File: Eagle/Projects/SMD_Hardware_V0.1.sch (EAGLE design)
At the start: 3 parts, among them IC1 LM386M-1

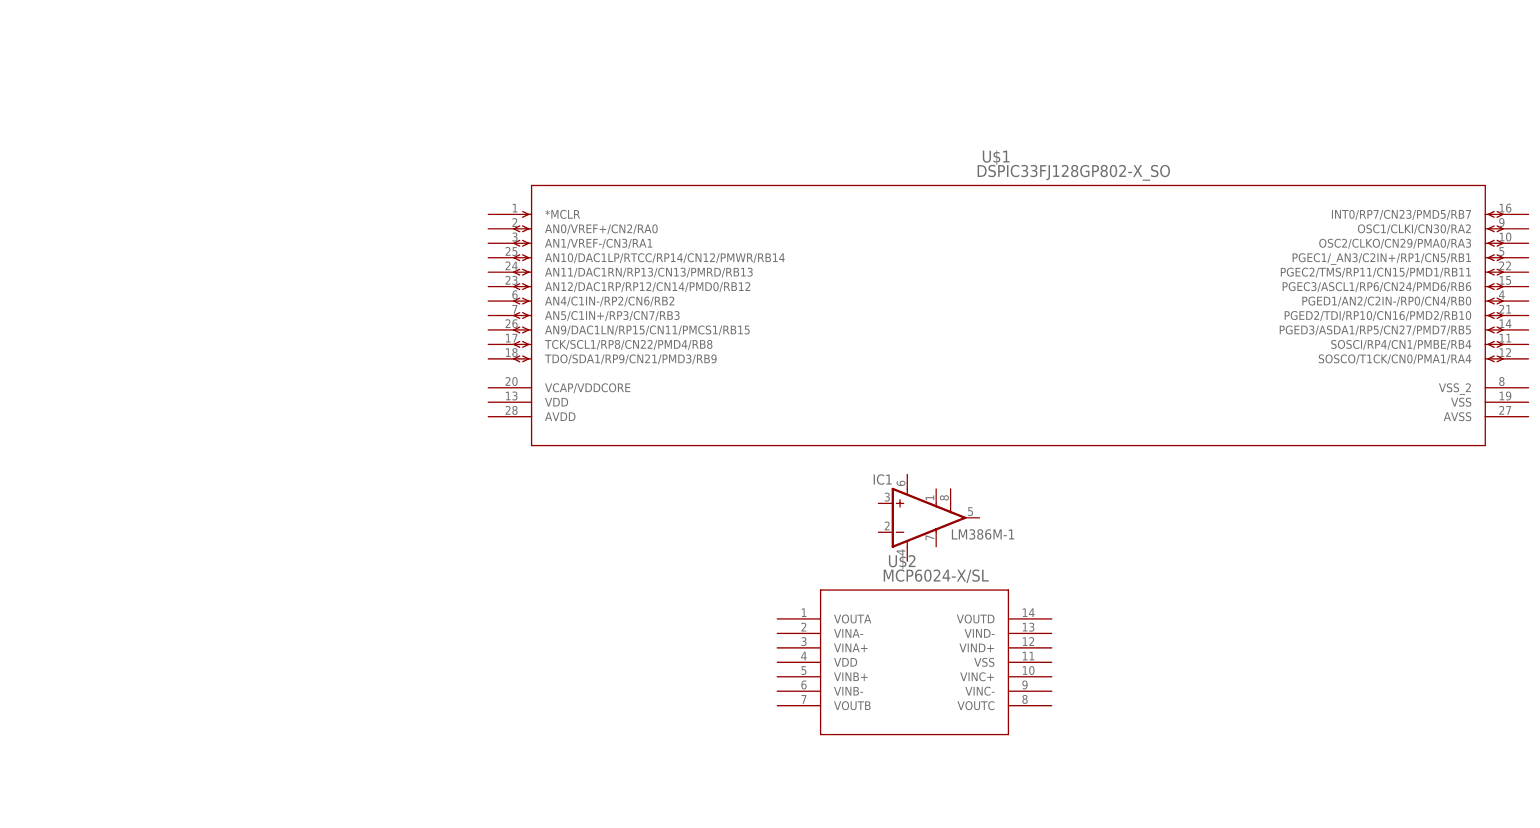
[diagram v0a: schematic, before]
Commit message: Layed out the board a bit more, finished off some connections for the basic micro layout.  Need to add a power supply yet
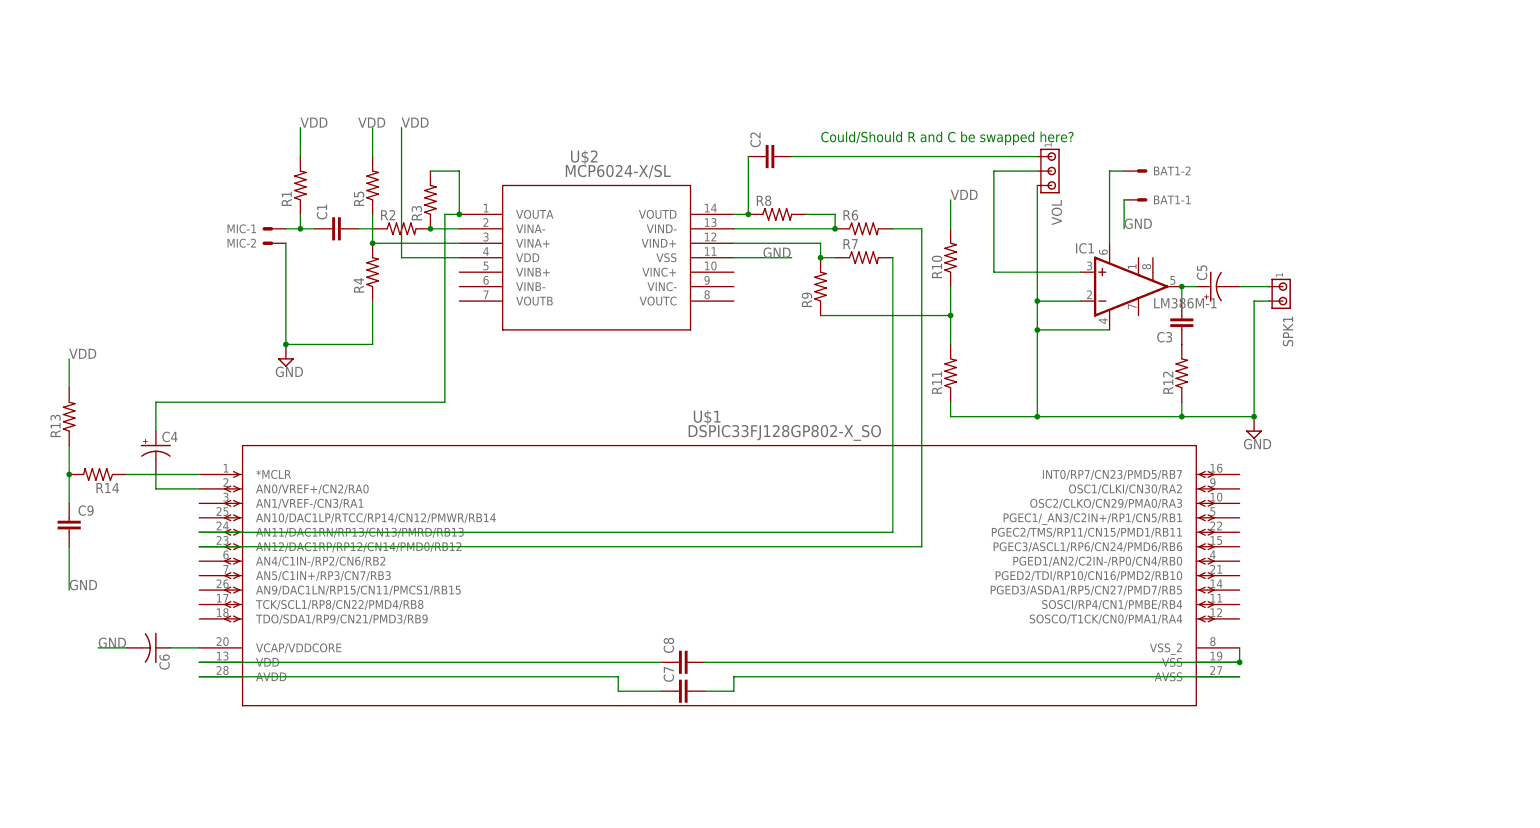
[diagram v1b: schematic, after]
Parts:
- added BAT1, MIC: 22-23-2021, con-molex:22-23-2021
- added C1, C2, C3: (no value), resistor:C-EUC0603
- added C4, C5: (no value), resistor:CPOL-US140CLH-0810
- added C6: (no value), resistor:C-USC0805
- added C7, C8, C9: (no value), resistor:C-EUC0805
- added R1, R10, R11, R12, R13, R14, R2, R3, R4, R5, R6, R7, R8, R9: (no value), resistor:R-US_R0603
- added SPK1: (no value), con-amp:MTA02-100
- added VOL: (no value), con-amp:MTA03-100
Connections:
- new net GND: BAT1-1.S, C6.2, C9.2, IC1.-IN, IC1.GND, MIC-2.S, R11.1, R12.1, R4.1, SPK1.2, U$2.VSS, VOL.3
- new net N$1: C1.1, MIC-1.S, R1.1
- new net N$10: R7.1, R9.2, U$2.VIND+
- new net N$11: R6.2, U$1.AN12/DAC1RP/RP12/CN14/PMD0/RB12
- new net N$12: C4.-, U$1.AN0/VREF+/CN2/RA0
- new net N$13: BAT1-2.S, IC1.VS
- new net N$14: C2.2, VOL.1
- new net N$15: C3.2, C5.+, IC1.OUT
- new net N$16: C3.1, R12.2
- new net N$17: C5.-, SPK1.1
- new net N$18: C6.1, U$1.VCAP/VDDCORE
- new net N$19: C8.1, U$1.VDD
- new net N$2: C1.2, R2.1
- new net N$20: C8.2, U$1.VSS, U$1.VSS_2
- new net N$21: C7.1, U$1.AVDD
- new net N$22: C7.2, U$1.AVSS
- new net N$23: C9.1, R13.1, R14.2
- new net N$24: R14.1, U$1.*MCLR
- new net N$25: IC1.+IN, VOL.2
- new net N$3: R2.2, R3.1, U$2.VINA-
- new net N$4: R4.2, R5.1, U$2.VINA+
- new net N$5: R10.1, R11.2, R9.1
- new net N$6: C4.+, R3.2, U$2.VOUTA
- new net N$7: C2.1, R8.1, U$2.VOUTD
- new net N$8: R6.1, R8.2, U$2.VIND-
- new net N$9: R7.2, U$1.AN11/DAC1RN/RP13/CN13/PMRD/RB13
- new net VDD: R1.2, R10.2, R13.2, R5.2, U$2.VDD
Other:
- note added: "Could/Should R and C be swapped here?"
- moved on the sheet: IC1, U$1, U$2

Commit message: Started editing the eagle files with values from the breadboard, and was working on the code a bit more
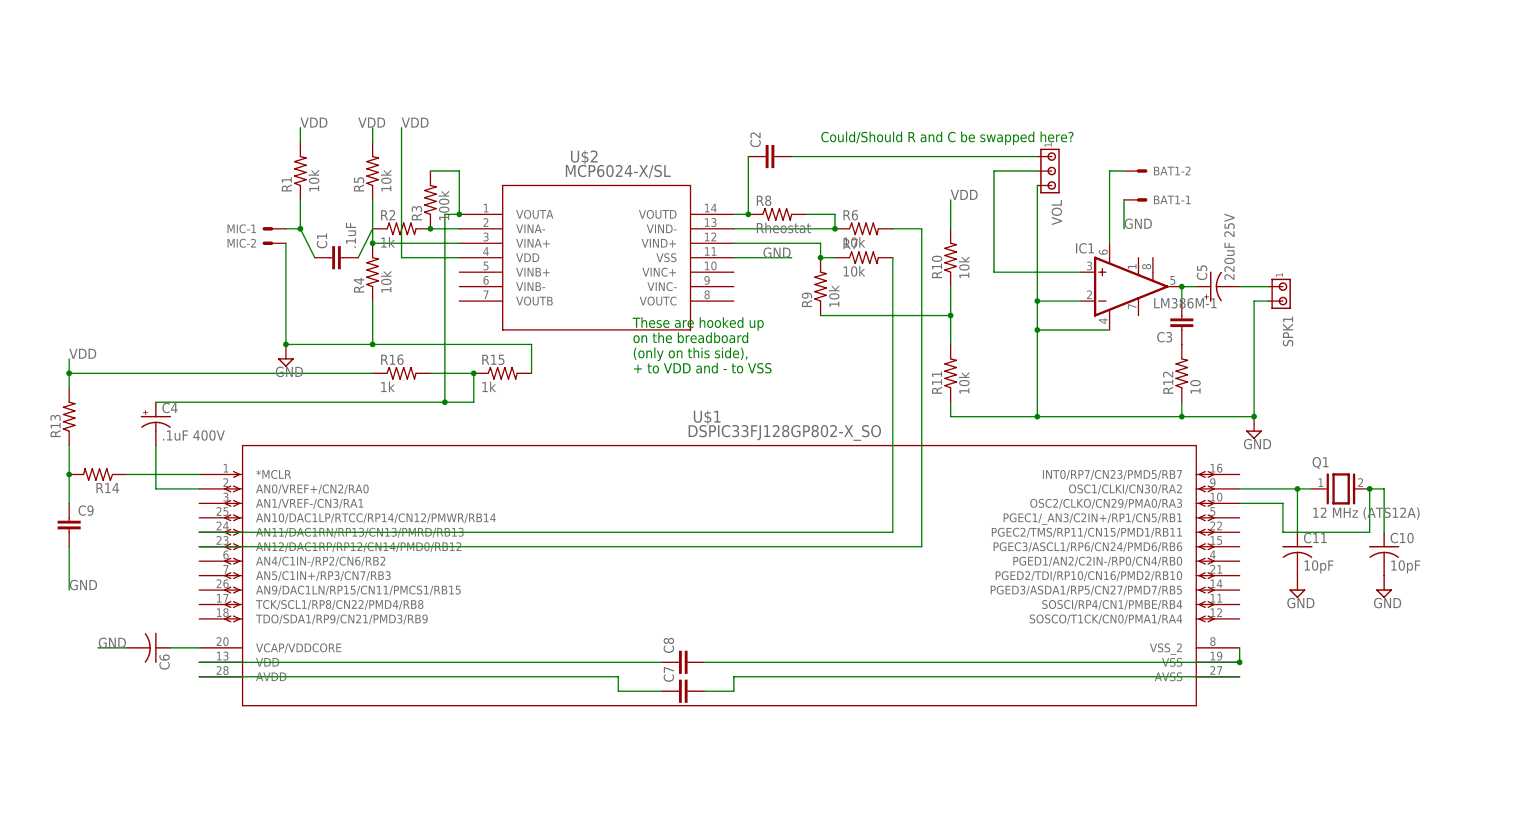
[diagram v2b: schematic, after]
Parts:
- added C10, C11: 10pF, resistor:C-US025-024X044
- added Q1: 12 MHz (ATS12A), special:XTAL
- added R15, R16: 1k, resistor:R-US_R0603
- C1: value (none) -> .1uF
- C4: value (none) -> .1uF 400V
- C5: value (none) -> 220uF 25V
- R1, R10, R11, R4, R5, R6, R7, R9: value (none) -> 10k
- R12: value (none) -> 10
- R2: value (none) -> 1k
- R3: value (none) -> 100k
- R8: value (none) -> Rheostat
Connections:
- removed net N$6: C4.+, R3.2, U$2.VOUTA
- new net N$26: C4.+, R15.1, R16.2, R3.2, U$2.VOUTA
- new net N$28: C11.1, Q1.1, U$1.OSC1/CLKI/CN30/RA2
- new net N$29: C10.1, Q1.2, U$1.OSC2/CLKO/CN29/PMA0/RA3
- net GND: now also C10.2, C11.2, R15.2
- net VDD: now also R16.1
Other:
- note added: "These are hooked up on the breadboard (only on this side), + to VDD and - to VSS"
- moved on the sheet: C1, C4, R1, R5

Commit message: Eagle changes
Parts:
- C9: value (none) -> DNI
- R13: value (none) -> 10k
- R14: value (none) -> 0 (short)
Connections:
- new net N$27: U$1.PGED1/AN2/C2IN-/RP0/CN4/RB0
- new net N$6: U$1.PGEC1/_AN3/C2IN+/RP1/CN5/RB1
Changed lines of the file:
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@@
 <part name="C7" library="resistor" deviceset="C-EU" device="C0805"/>
 <part name="C8" library="resistor" deviceset="C-EU" device="C0805"/>
-<part name="C9" library="resistor" deviceset="C-EU" device="C0805"/>
-<part name="R13" library="resistor" deviceset="R-US_" device="R0603"/>
-<part name="R14" library="resistor" deviceset="R-US_" device="R0603"/>
+<part name="C9" library="resistor" deviceset="C-EU" device="C0805" value="DNI"/>
+<part name="R13" library="resistor" deviceset="R-US_" device="R0603" value="10k"/>
+<part name="R14" library="resistor" deviceset="R-US_" device="R0603" value="0 (short)"/>
 <part name="SUPPLY1" library="supply2" deviceset="GND" device=""/>
 <part name="SUPPLY2" library="supply2" deviceset="GND" device=""/>
@@
 </segment>
 </net>
+<net name="N$6" class="0">
+<segment>
+<pinref part="U$1" gate="A" pin="PGEC1/_AN3/C2IN+/RP1/CN5/RB1"/>
+<wire x1="142.24" y1="43.18" x2="147.32" y2="43.18" width="0.1524" layer="91"/>
+<wire x1="147.32" y1="43.18" x2="147.32" y2="53.34" width="0.1524" layer="91"/>
+<wire x1="147.32" y1="53.34" x2="152.4" y2="53.34" width="0.1524" layer="91"/>
+<wire x1="152.4" y1="53.34" x2="152.4" y2="68.58" width="0.1524" layer="91"/>
+<wire x1="152.4" y1="68.58" x2="165.1" y2="68.58" width="0.1524" layer="91"/>
+</segment>
+</net>
+<net name="N$27" class="0">
+<segment>
+<pinref part="U$1" gate="A" pin="PGED1/AN2/C2IN-/RP0/CN4/RB0"/>
+<wire x1="142.24" y1="35.56" x2="144.78" y2="35.56" width="0.1524" layer="91"/>
+<wire x1="144.78" y1="35.56" x2="144.78" y2="50.8" width="0.1524" layer="91"/>
+<wire x1="144.78" y1="50.8" x2="154.94" y2="50.8" width="0.1524" layer="91"/>
+<wire x1="154.94" y1="50.8" x2="154.94" y2="66.04" width="0.1524" layer="91"/>
+<wire x1="154.94" y1="66.04" x2="165.1" y2="66.04" width="0.1524" layer="91"/>
+</segment>
+</net>

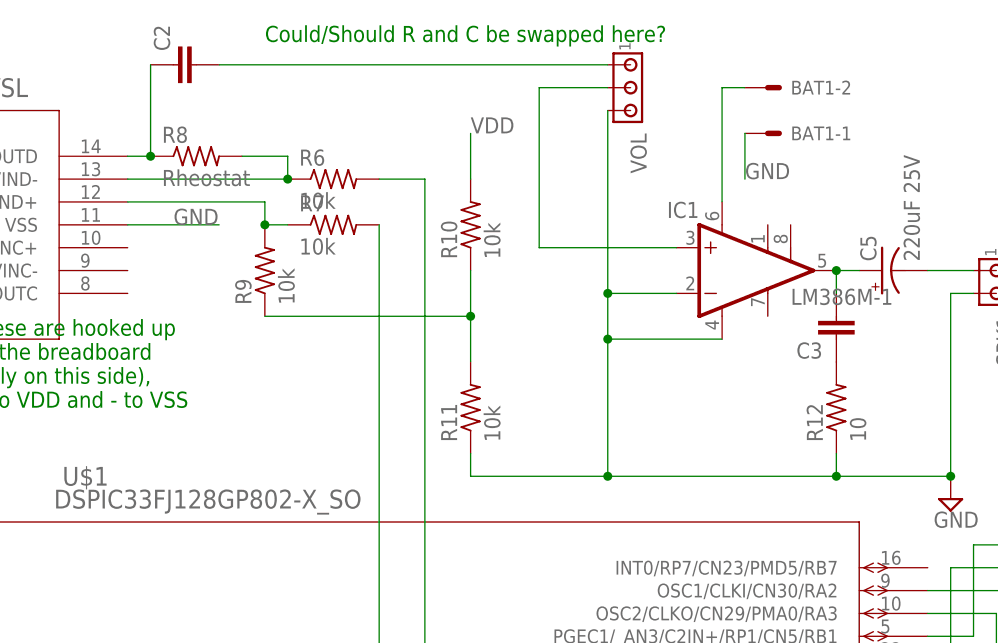
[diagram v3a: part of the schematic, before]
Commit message: Updated the schematic a bit, lowered the ADC gain to not use digital gain.  Trying to improve the analog to take care of this
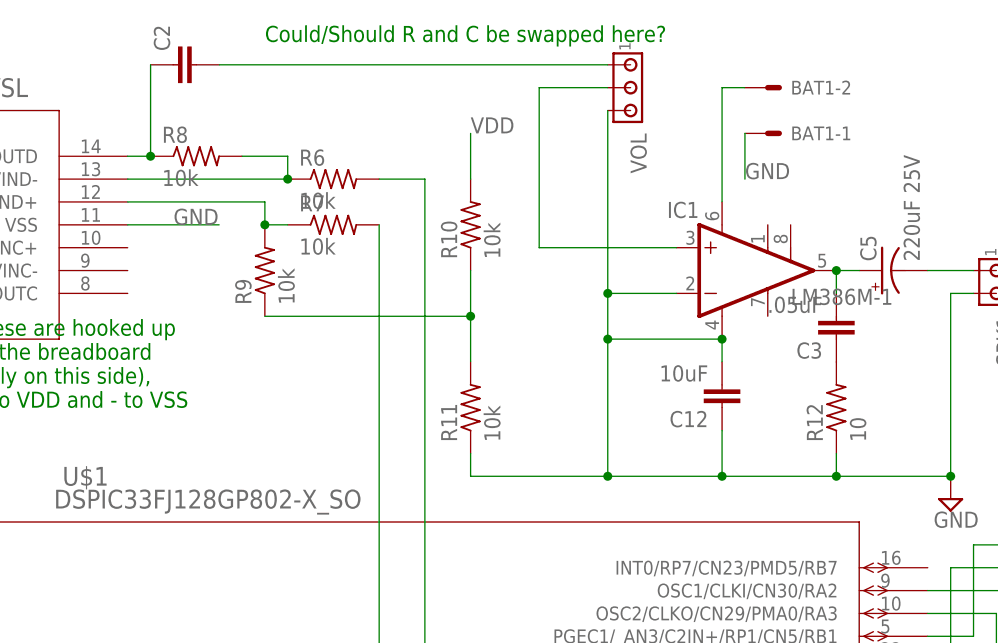
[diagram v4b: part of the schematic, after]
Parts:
- added C12: 10uF, resistor:C-EUC0603
- C3: value (none) -> .05uF
- R8: value Rheostat -> 10k
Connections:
- net GND: now also C12.1, C12.2
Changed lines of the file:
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@@
 <part name="R6" library="resistor" deviceset="R-US_" device="R0603" value="10k"/>
 <part name="R7" library="resistor" deviceset="R-US_" device="R0603" value="10k"/>
-<part name="R8" library="resistor" deviceset="R-US_" device="R0603" value="Rheostat"/>
+<part name="R8" library="resistor" deviceset="R-US_" device="R0603" value="10k"/>
 <part name="R9" library="resistor" deviceset="R-US_" device="R0603" value="10k"/>
 <part name="R10" library="resistor" deviceset="R-US_" device="R0603" value="10k"/>
@@
 <part name="C4" library="resistor" deviceset="CPOL-US" device="140CLH-0810" value=".1uF 400V"/>
 <part name="BAT1" library="con-molex" deviceset="22-23-2021" device="" value=""/>
-<part name="C3" library="resistor" deviceset="C-EU" device="C0603"/>
+<part name="C3" library="resistor" deviceset="C-EU" device="C0603" value=".05uF"/>
 <part name="C5" library="resistor" deviceset="CPOL-US" device="140CLH-0810" value="220uF 25V"/>
 <part name="R12" library="resistor" deviceset="R-US_" device="R0603" value="10"/>
@@
 <part name="SUPPLY3" library="supply2" deviceset="GND" device=""/>
 <part name="SUPPLY4" library="supply2" deviceset="GND" device=""/>
+<part name="C12" library="resistor" deviceset="C-EU" device="C0603" value="10uF"/>
 </parts>
 <sheets>
@@
 <instance part="SUPPLY3" gate="GND" x="152.4" y="30.48"/>
 <instance part="SUPPLY4" gate="GND" x="167.64" y="30.48"/>
+<instance part="C12" gate="G$1" x="119.38" y="68.58" rot="R180"/>
 </instances>
 <busses>
@@
 <wire x1="91.44" y1="63.5" x2="91.44" y2="60.96" width="0.1524" layer="91"/>
 <wire x1="91.44" y1="60.96" x2="106.68" y2="60.96" width="0.1524" layer="91"/>
-<wire x1="106.68" y1="60.96" x2="132.08" y2="60.96" width="0.1524" layer="91"/>
+<wire x1="106.68" y1="60.96" x2="119.38" y2="60.96" width="0.1524" layer="91"/>
 <junction x="106.68" y="60.96"/>
 <pinref part="R12" gate="G$1" pin="1"/>
+<wire x1="119.38" y1="60.96" x2="132.08" y2="60.96" width="0.1524" layer="91"/>
 <wire x1="132.08" y1="60.96" x2="132.08" y2="63.5" width="0.1524" layer="91"/>
 <pinref part="SPK1" gate="G$1" pin="2"/>
@@
 <pinref part="SUPPLY2" gate="GND" pin="GND"/>
 <junction x="144.78" y="60.96"/>
+<pinref part="C12" gate="G$1" pin="2"/>
+<wire x1="119.38" y1="76.2" x2="119.38" y2="73.66" width="0.1524" layer="91"/>
+<junction x="119.38" y="76.2"/>
+<pinref part="C12" gate="G$1" pin="1"/>
+<wire x1="119.38" y1="66.04" x2="119.38" y2="60.96" width="0.1524" layer="91"/>
+<junction x="119.38" y="60.96"/>
 </segment>
 <segment>
